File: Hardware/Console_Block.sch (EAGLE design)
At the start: 39 parts, among them Q1 BSS138, U2 FTS31XS-U, U4 TPS62065

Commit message: file cleanup
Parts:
- L1: value (none) -> 1.0uH
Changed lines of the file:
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@@
 <part name="C4" library="SparkFun-Capacitors" deviceset="47PF-50V-5%(0603)" device="" value="47pF"/>
 <part name="SUPPLY1" library="SparkFun-Aesthetics" deviceset="5V" device=""/>
-<part name="SUPPLY2" library="SparkFun-Aesthetics" deviceset="5V" device=""/>
 <part name="SUPPLY3" library="SparkFun-Aesthetics" deviceset="5V" device=""/>
 <part name="GND8" library="SparkFun-Aesthetics" deviceset="GND" device=""/>
@@
 <part name="C10" library="SparkFun-Capacitors" deviceset="4.7UF-6.3V-10%(0603)" device="0603" value="4.7uF"/>
 <part name="GND19" library="SparkFun-Aesthetics" deviceset="GND" device=""/>
-<part name="L1" library="SparkFun-Passives" deviceset="INDUCTOR" device=""/>
+<part name="L1" library="SparkFun-Passives" deviceset="INDUCTOR" device="" value="1.0uH"/>
 <part name="FID1" library="SparkFun-Aesthetics" deviceset="FIDUCIAL" device="1X2"/>
 <part name="FID2" library="SparkFun-Aesthetics" deviceset="FIDUCIAL" device="1X2"/>
@@
 <instance part="C4" gate="G$1" x="53.34" y="129.54"/>
 <instance part="SUPPLY1" gate="G$1" x="71.12" y="152.4"/>
-<instance part="SUPPLY2" gate="G$1" x="40.64" y="147.32"/>
 <instance part="SUPPLY3" gate="G$1" x="40.64" y="147.32"/>
 <instance part="GND8" gate="1" x="45.72" y="121.92" rot="MR0"/>
@@
 </segment>
 <segment>
-<pinref part="SUPPLY2" gate="G$1" pin="5V"/>
 <pinref part="SUPPLY3" gate="G$1" pin="5V"/>
 <pinref part="JP1" gate="G$1" pin="VCC"/>
@@
 <wire x1="83.82" y1="88.9" x2="83.82" y2="91.44" width="0.1524" layer="91"/>
 <junction x="114.3" y="91.44"/>
-</segment>
-<segment>
+<junction x="101.6" y="91.44"/>
+</segment>
+<segment>

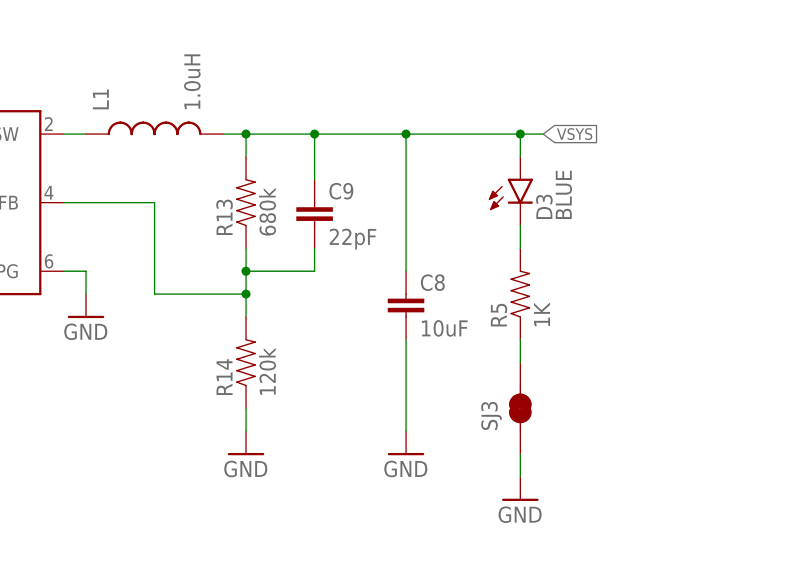
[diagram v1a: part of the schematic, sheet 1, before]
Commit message: changed rev number to v01 replaced ouput capacitor on vreg to 22uF replaced filter capacitor on vreg to 47pf replaced connector footprints to add T/Brestrict to prevent solder bridging
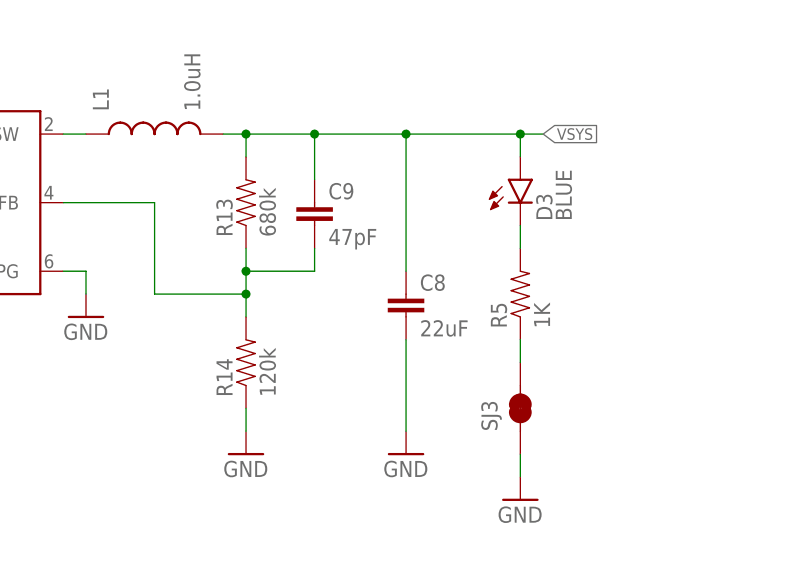
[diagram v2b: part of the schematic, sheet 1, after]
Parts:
- C8: value 10uF -> 22uF; device SparkFun-Capacitors:10UF-6.3V-20%(1206) -> SparkFun-Capacitors:22UF-6.3V-20%(0805)
- C9: value 22pF -> 47pF; device SparkFun-Capacitors:22PF-50V-5%(0603) -> SparkFun-Capacitors:47PF-50V-5%(0603)
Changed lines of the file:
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@@
 <?xml version="1.0" encoding="utf-8"?>
 <!DOCTYPE eagle SYSTEM "eagle.dtd">
-<eagle version="6.5.0">
+<eagle version="6.6.0">
 <drawing>
 <settings>
@@
 <part name="GND15" library="SparkFun-Aesthetics" deviceset="GND" device=""/>
 <part name="GND16" library="SparkFun-Aesthetics" deviceset="GND" device=""/>
-<part name="C8" library="SparkFun-Capacitors" deviceset="10UF-6.3V-20%(1206)" device="" value="10uF"/>
+<part name="C8" library="SparkFun-Capacitors" deviceset="22UF-6.3V-20%(0805)" device="" value="22uF"/>
 <part name="GND18" library="SparkFun-Aesthetics" deviceset="GND" device=""/>
 <part name="U4" library="Testing" deviceset="TPS62065" device=""/>
@@
 <part name="R13" library="SparkFun-Resistors" deviceset="RESISTOR" device="0603" value="680k"/>
 <part name="R14" library="SparkFun-Resistors" deviceset="RESISTOR" device="0603" value="120k"/>
-<part name="C9" library="SparkFun-Capacitors" deviceset="22PF-50V-5%(0603)" device="" value="22pF"/>
+<part name="C9" library="SparkFun-Capacitors" deviceset="47PF-50V-5%(0603)" device="" value="47pF"/>
 <part name="C10" library="SparkFun-Capacitors" deviceset="4.7UF-6.3V-10%(0603)" device="0603" value="4.7uF"/>
 <part name="GND19" library="SparkFun-Aesthetics" deviceset="GND" device=""/>

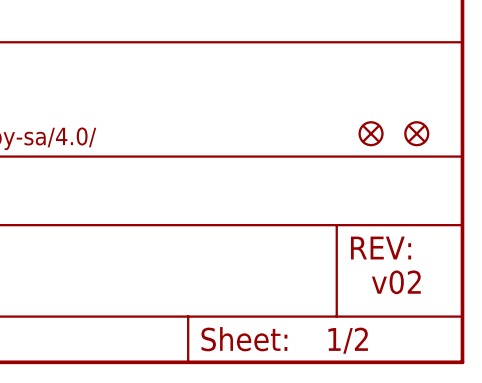
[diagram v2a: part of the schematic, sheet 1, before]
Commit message: fixed bridging
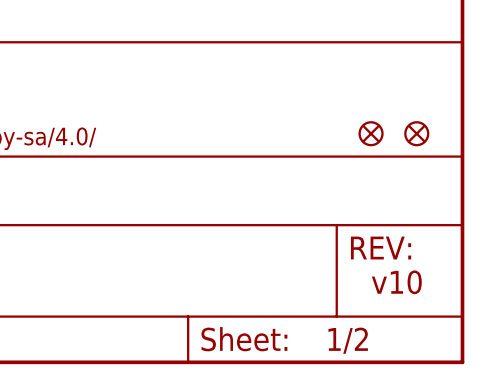
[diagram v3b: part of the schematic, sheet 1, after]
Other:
- note added: "v10"
- note removed: "v02"
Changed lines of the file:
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@@
 <sheet>
 <plain>
-<text x="238.76" y="7.62" size="2.54" layer="94">v02</text>
+<text x="238.76" y="7.62" size="2.54" layer="94">v10</text>
 <text x="170.18" y="7.62" size="2.54" layer="94">Casey Kuhns</text>
 <text x="177.8" y="88.9" size="1.27" layer="97">DCIN Enable Circuit
